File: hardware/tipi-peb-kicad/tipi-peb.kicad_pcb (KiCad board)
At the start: 2 copper layers, 237.7 x 117.3 mm, 44 parts, among them Q1 Q_NPN_BCE, U1 74HCT138, U2 27C256, U3 74HCT244, U4 74HCT244, U5 74HCT244, U6 XC95144XL-TQ100, U7 74HCT245, U8 LM1117-3.3, U9 LM7805_TO220

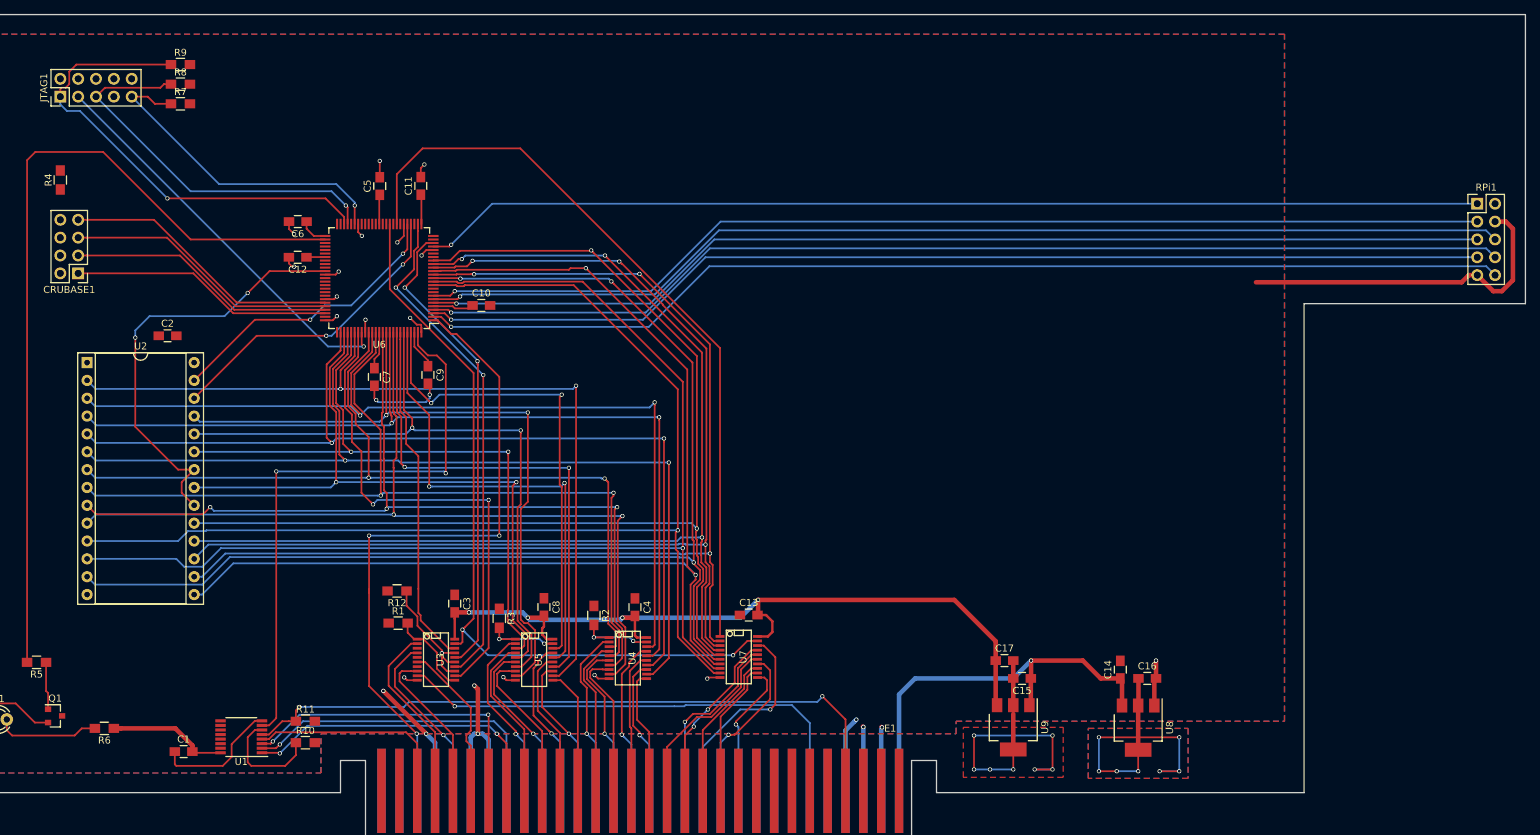
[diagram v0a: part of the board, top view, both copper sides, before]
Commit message: drc says it is good, status bar says 2 unconnected
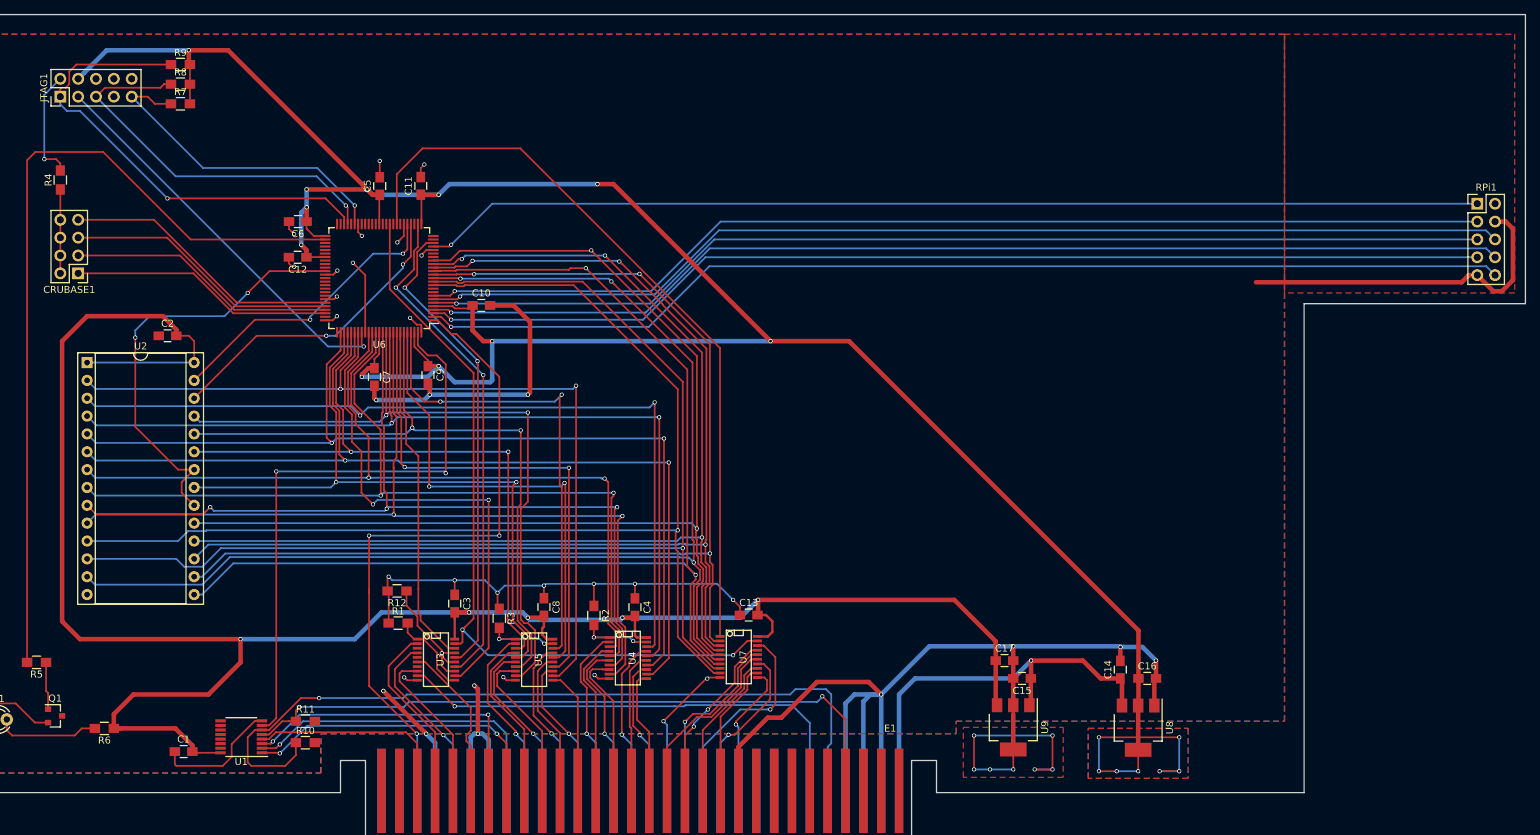
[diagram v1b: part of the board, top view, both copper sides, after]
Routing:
- net +3V3: track 77.6 -> 382.2 mm, vias 7 -> 18
- net GND: track 243.4 -> 485.9 mm, vias 33 -> 43
- net +5V: track 134.0 -> 301.4 mm, vias 4 -> 5
- net TI_AME: track 15.5 -> 113.2 mm, vias 0 -> 1
- net Net-(CRUBASE1-Pad1): track 0.00 -> 11.9 mm

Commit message: adjust page layout
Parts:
- moved C1 77.0 mm to (66.6, 142.7)
- moved C10 77.0 mm to (108.9, 79.2)
- moved C13 77.0 mm to (147.0, 123.3)
- moved C14 77.0 mm to (199.9, 131.1)
- moved C15 77.0 mm to (185.9, 132.3)
- moved C17 77.0 mm to (183.4, 129.8)
- moved C5 77.0 mm to (94.5, 62.2)
- moved C7 77.0 mm to (93.7, 89.4)
- moved C8 77.0 mm to (117.9, 122.2)
- moved JTAG1 77.0 mm to (49.0, 49.5)
- moved R4 77.0 mm to (49.0, 61.4)
- moved RPi1 77.0 mm to (250.7, 64.8)
- moved U4 77.0 mm to (129.8, 129.4)
- moved U6 77.0 mm to (94.4, 75.4)
- moved U9 77.0 mm to (184.7, 139.3)
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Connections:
- R10 pad 2: Net-(R10-Pad2) -> +5V
- R11 pad 2: Net-(R11-Pad2) -> GND
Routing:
- net +5V: track 301.4 -> 321.9 mm
- net GND: track 485.9 -> 471.1 mm, vias 43 -> 44
- net TI_AME: track 113.2 -> 111.7 mm

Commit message: room to mount a PI 3
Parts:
- added REF**: MountingHole_3.2mm_M3, Mounting_Holes:MountingHole_3.2mm_M3, F.Cu at (138.2, 78.7)
- added REF**: MountingHole_3.2mm_M3, Mounting_Holes:MountingHole_3.2mm_M3, F.Cu at (196.1, 78.7)
- added REF**: MountingHole_3.2mm_M3, Mounting_Holes:MountingHole_3.2mm_M3, F.Cu at (138.2, 30.0)
- added REF**: MountingHole_3.2mm_M3, Mounting_Holes:MountingHole_3.2mm_M3, F.Cu at (196.1, 29.7)
- moved C1 15.8 mm to (65.8, 158.5)
- moved D1 15.8 mm to (38.1, 153.9)
- moved U4 15.8 mm to (129.0, 145.2)
- moved U8 15.8 mm to (201.7, 155.1)
- moved C12 15.8 mm to (82.0, 88.1)
- moved C4 15.8 mm to (130.0, 137.9)
- moved C5 15.8 mm to (93.7, 78.0)
- moved C6 15.8 mm to (82.1, 83.1)
- moved C7 15.8 mm to (93.0, 105.2)
- moved C9 15.8 mm to (100.6, 104.9)
- moved CRUBASE1 15.8 mm to (50.8, 90.4)
- moved JTAG1 15.8 mm to (48.3, 65.3)
- moved R1 15.8 mm to (96.3, 140.2)
- moved R3 15.8 mm to (110.7, 139.5)
- moved R9 15.8 mm to (65.4, 60.7)
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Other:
- board size 237.7 x 117.3 mm -> 237.7 x 146.1 mm

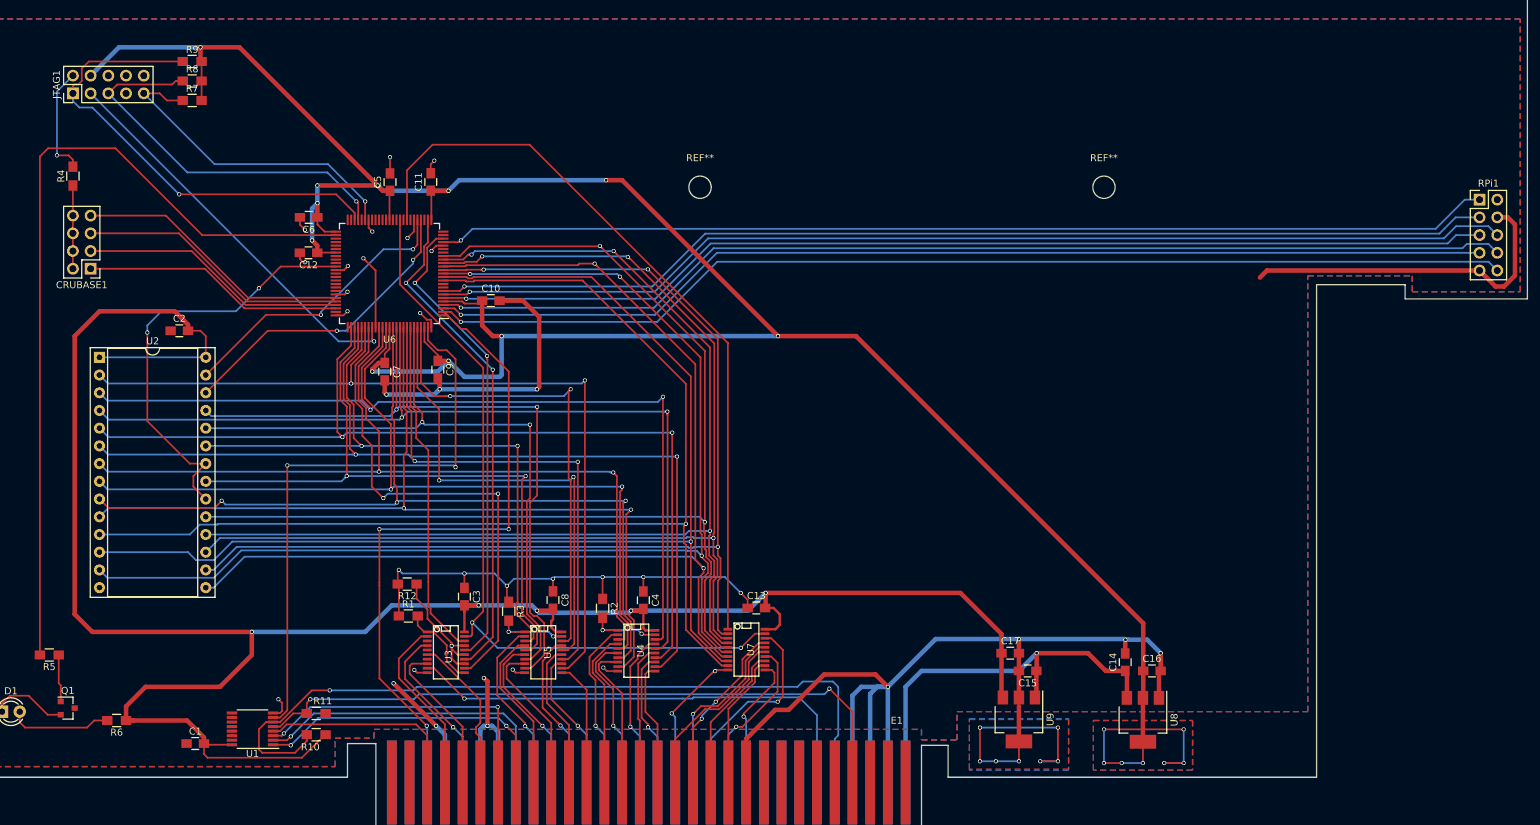
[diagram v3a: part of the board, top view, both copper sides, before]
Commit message: Fix to work on 4A.
Jumper added to disconnect SCLK/AMD line on 4As.
Pull-up resister added to boost power on r_din transmission line.
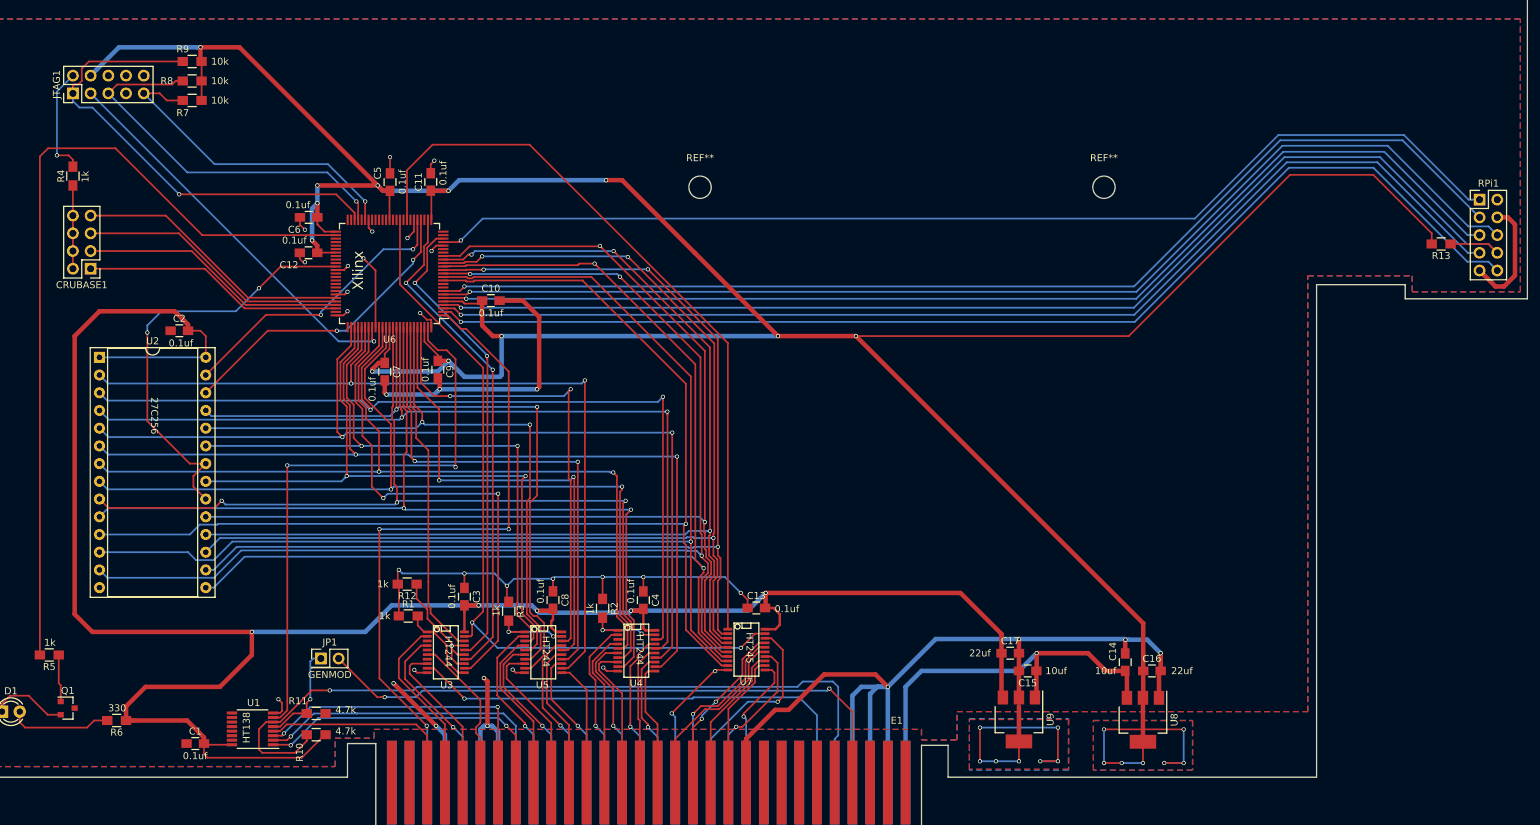
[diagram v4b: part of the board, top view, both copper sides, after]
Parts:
- added JP1: GENMOD, Pin_Headers:Pin_Header_Straight_2x01_Pitch2.54mm, F.Cu at (83.8, 146.3)
- added R13: 10k, Resistors_SMD:R_0805_HandSoldering, F.Cu at (244.4, 86.9)
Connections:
- R11 pad 1: TI_AMD -> Net-(JP1-Pad1)
- U1 pad 5: TI_AMD -> Net-(JP1-Pad1)
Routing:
- net +3V3: track 382.2 -> 479.3 mm, vias 18 -> 19
- net GND: track 471.1 -> 439.2 mm
- net R_DIN: track 155.6 -> 173.1 mm
- net Net-(JP1-Pad1): track 0.00 -> 15.0 mm, vias 0 -> 1
- net R_DC: track 155.8 -> 167.0 mm
- net R_RESET: track 152.6 -> 163.4 mm
- net R_LE: track 152.4 -> 162.3 mm
- net TI_AMD: track 97.8 -> 88.0 mm
- net R_DOUT: track 155.7 -> 165.3 mm
- net R_RT: track 153.0 -> 162.1 mm
- net R_CLK: track 151.1 -> 158.8 mm
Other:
- board text added: "0.1uf"
- board text added: "10k"
- board text added: "10uf"
- board text added: "1k"
- board text added: "22uf"
- board text added: "27C256"
- board text added: "330"
- board text added: "4.7k"
- board text added: "HT138"
- board text added: "HT244"
- board text added: "HT245"
- board text added: "Xilinx"

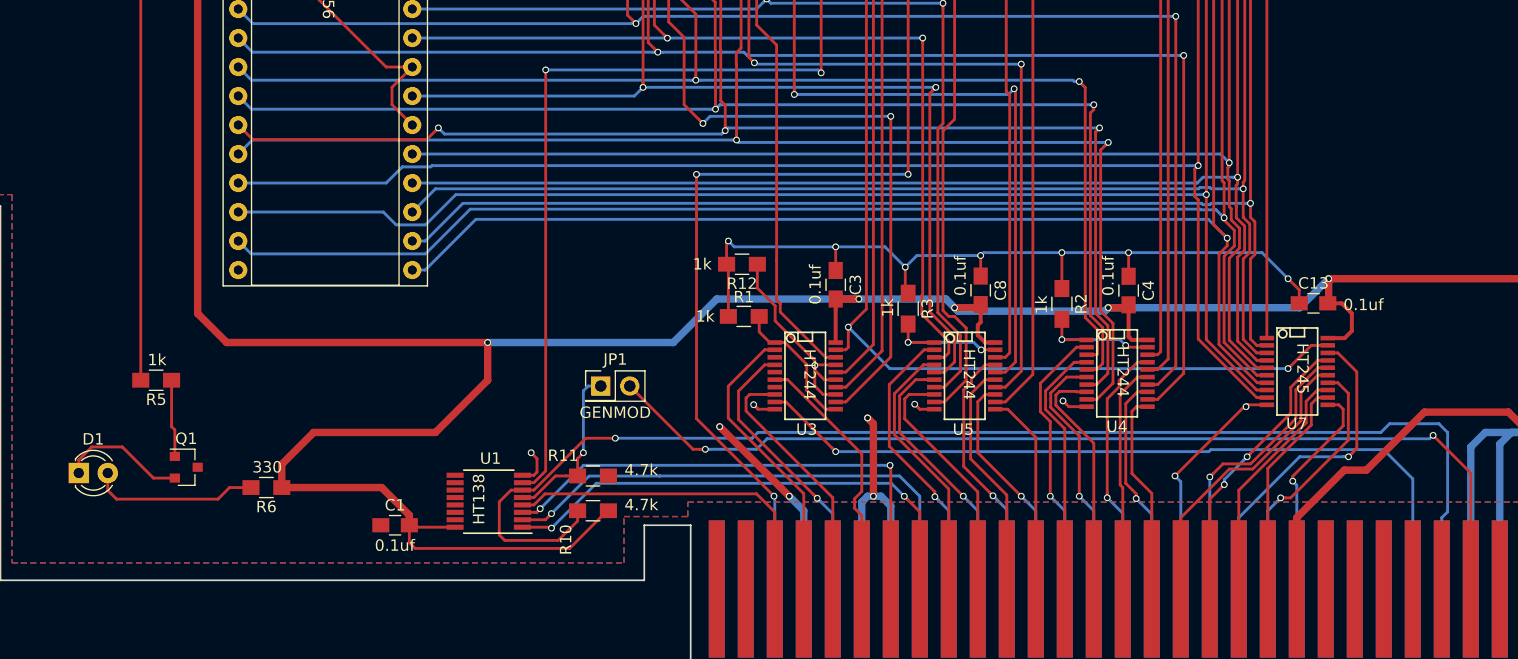
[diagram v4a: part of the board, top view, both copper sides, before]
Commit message: Add solder jumpers for genmod vs standard support.
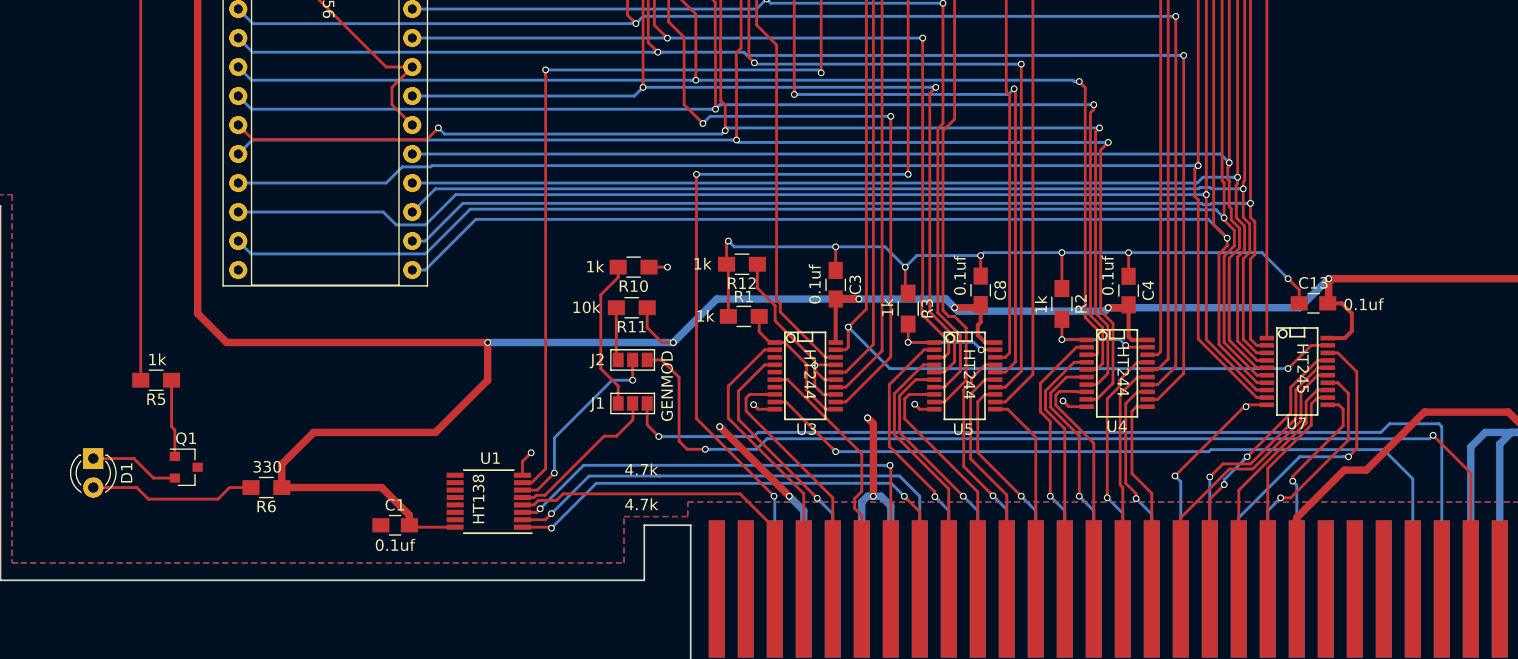
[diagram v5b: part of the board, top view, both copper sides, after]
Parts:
- removed JP1: GENMOD, Pin_Headers:Pin_Header_Straight_2x01_Pitch2.54mm
- added J1: GS3, Connectors:GS3, F.Cu at (86.6, 147.8)
- added J2: GS3, Connectors:GS3, F.Cu at (86.6, 144.0)
- R10: value 4.7k -> 1k
- R11: value 4.7k -> 10k
- moved R10 21.6 mm to (86.7, 135.9), turned to 180 degrees
- moved R11 15.1 mm to (86.5, 139.4), turned to 180 degrees
- moved D1 1.80 mm to (39.4, 152.7), turned to 270 degrees
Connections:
- R10 pad 1: TI_AME -> GND
- R10 pad 2: +5V -> Net-(J1-Pad1)
- R11 pad 1: Net-(JP1-Pad1) -> +5V
- R11 pad 2: GND -> Net-(J2-Pad1)
- U1 pad 5: Net-(JP1-Pad1) -> Net-(J1-Pad2)
- U1 pad 6: TI_AME -> Net-(J2-Pad2)
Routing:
- net TI_AME: track 111.7 -> 86.7 mm
- net Net-(J2-Pad2): track 0.00 -> 17.2 mm, vias 0 -> 2
- net +5V: track 321.9 -> 306.0 mm, vias 5 -> 6
- net Net-(JP1-Pad1): track 15.0 -> 0.00 mm, vias 1 -> 0
- net Net-(J1-Pad2): track 0.00 -> 13.9 mm
- net Net-(J1-Pad1): track 0.00 -> 13.2 mm
- net Net-(J2-Pad1): track 0.00 -> 4.64 mm
- net Net-(D1-Pad1): track 11.2 -> 7.85 mm
- net TI_AMD: track 88.0 -> 90.7 mm
- net TI_MEMEN: track 29.9 -> 29.1 mm
- net GND: track 439.2 -> 439.8 mm, vias 44 -> 45
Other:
- board text added: "GENMOD"

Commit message: little changes to silks
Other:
- board text added: "8 4 2 1"
- board text added: ">1?00"
- board text added: "T"
- board text added: "ipiPEB"
- board text added: "rev2 - ti994a.cwfk.net"
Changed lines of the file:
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@@
   (general
     (links 226)
-    (no_connects 8)
-    (area 18.974999 24.543 257.858381 171.017001)
+    (no_connects 0)
+    (area 18.974999 24.816999 256.869001 171.017001)
     (thickness 1.6)
-    (drawings 62)
+    (drawings 72)
     (tracks 1531)
     (zones 0)
@@
     )
   )
+  (gr_text "rev2 - ti994a.cwfk.net" (at 191.008 124.206) (layer F.SilkS)
+    (effects (font (size 1.5 1.5) (thickness 0.3)))
+  )
+  (gr_line (start 160 103) (end 204.216 103) (layer F.SilkS) (width 0.5))
+  (gr_text T (at 156.464 110) (layer F.SilkS)
+    (effects (font (size 12.7 12.7) (thickness 0.5)))
+  )
+  (gr_text ipiPEB (at 182.88 111.252) (layer F.SilkS)
+    (effects (font (size 10 10) (thickness 0.5)))
+  )
+  (gr_text "8\n4\n2\n1" (at 41.656 86.614) (layer F.SilkS)
+    (effects (font (size 1.5 1.5) (thickness 0.3)))
+  )
+  (gr_line (start 45.72 90.424) (end 42.672 90.424) (layer F.SilkS) (width 0.2))
+  (gr_line (start 45.72 87.884) (end 42.672 87.884) (layer F.SilkS) (width 0.2))
+  (gr_line (start 45.72 85.344) (end 42.672 85.344) (layer F.SilkS) (width 0.2))
+  (gr_line (start 45.72 82.804) (end 42.672 82.804) (layer F.SilkS) (width 0.2))
+  (gr_text >1?00 (at 41.402 80.264) (layer F.SilkS)
+    (effects (font (size 1.5 1.5) (thickness 0.3)))
+  )
   (gr_text GENMOD (at 89.662 146.304 90) (layer F.SilkS)
